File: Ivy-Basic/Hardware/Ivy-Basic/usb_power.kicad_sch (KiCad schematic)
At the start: 1 part, among them J1 USB_C_Receptacle_USB2.0_16P

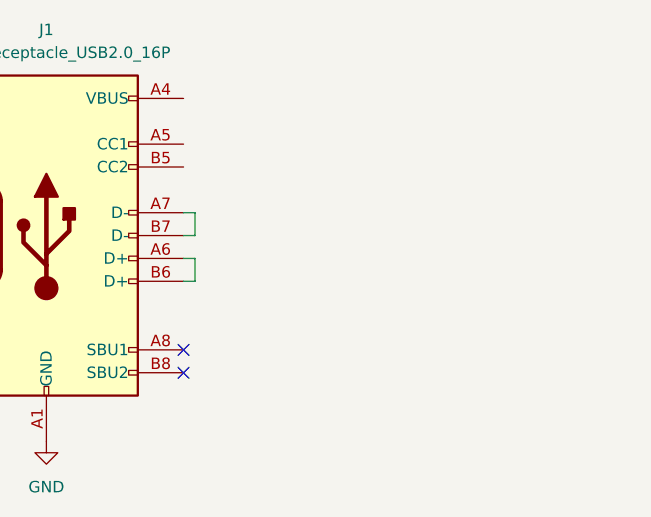
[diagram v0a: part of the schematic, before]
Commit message: Begin USB Power Sheet, ignore file locks, generate symbol library table
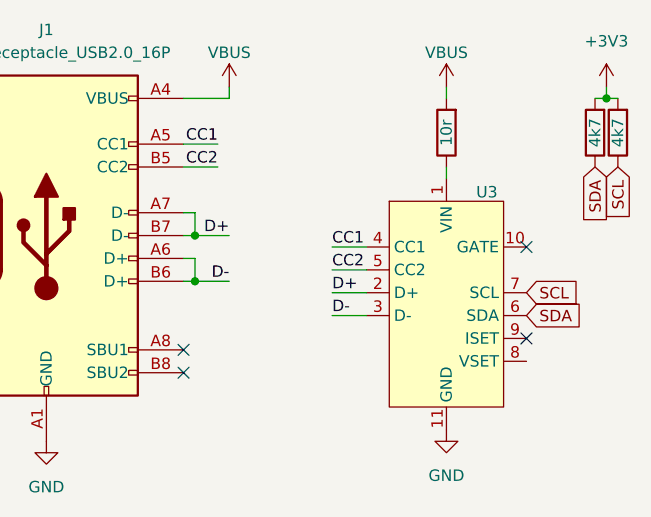
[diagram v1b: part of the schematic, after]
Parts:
- added R1: 10r, symbol Device:R
- added R2, R3: 4k7, symbol Device:R
- added U3: ~, symbol USB_Controller:HUSB238
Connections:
- net GND: now also U3.11 (GND)
- net VBUS: now reaches J1.A4 (VBUS), J1.A9 (VBUS), J1.B4 (VBUS), J1.B9 (VBUS)
- net VBUS: now also R1.2
- net CC1: now reaches J1.A5 (CC1)
- net CC1: now also U3.4 (CC1)
- net D-: now reaches J1.A6 (D+), J1.B6 (D+)
- net D-: now also U3.3 (D-)
- net D+: now reaches J1.A7 (D-), J1.B7 (D-)
- net D+: now also U3.2 (D+)
- net CC2: now reaches J1.B5 (CC2)
- net CC2: now also U3.5 (CC2)
- new net: R1.1, U3.1 (VIN)
- new net +3V3: R2.2, R3.2
- new net SCL: R3.1, U3.7 (SCL)
- new net SDA: R2.1, U3.6 (SDA)
- no-connect marks 2 -> 4

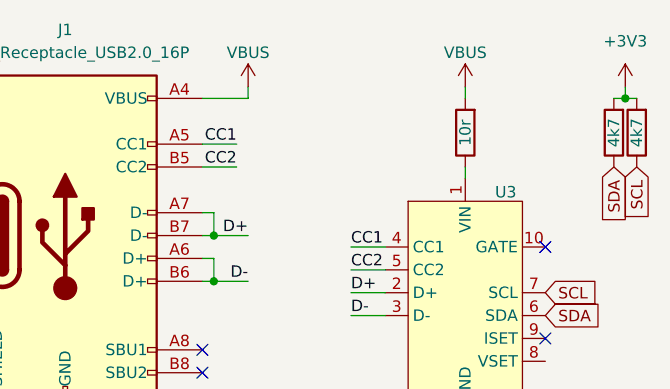
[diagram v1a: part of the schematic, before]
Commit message: USB PD Trigger Complete. Default to 20V.
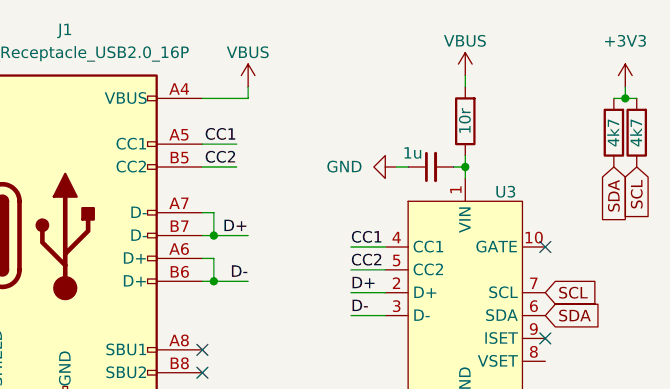
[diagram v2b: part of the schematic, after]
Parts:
- added C1: 1u, Capacitor_SMD:C_0402_1005Metric, symbol Device:C_Small
- J1: footprint (none) -> Connector_USB:USB_C_Receptacle_HRO_TYPE-C-31-M-12
- R1, R2, R3: footprint (none) -> Resistor_SMD:R_0402_1005Metric
- U3: footprint (none) -> Package_DFN_QFN:DFN-10-1EP_3x3mm_P0.5mm_EP1.7x2.5mm
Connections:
- net GND: now also C1.1
- net at R1.1, U3.1 (VIN): now also C1.2
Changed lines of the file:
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@@
+		(color 0 0 0 0)
+	)
+	(junction
+		(at 73.66 29.21)
+		(diameter 0)
 		(color 0 0 0 0)
 	)
@@
 	(wire
 		(pts
-			(xy 73.66 20.32) (xy 73.66 21.59)
+			(xy 72.39 29.21) (xy 73.66 29.21)
+		)
+		(stroke
+			(width 0)
+			(type default)
+		)
+	)
+	(wire
+		(pts
+			(xy 73.66 29.21) (xy 73.66 30.48)
+		)
+		(stroke
+			(width 0)
+			(type default)
+		)
+	)
+	(wire
+		(pts
+			(xy 73.66 19.05) (xy 73.66 20.32)
 		)
 		(stroke
@@
 	(wire
 		(pts
-			(xy 73.66 29.21) (xy 73.66 30.48)
+			(xy 73.66 27.94) (xy 73.66 29.21)
 		)
 		(stroke
@@
 		(pts
 			(xy 64.77 45.72) (xy 60.96 45.72)
+		)
+		(stroke
+			(width 0)
+			(type default)
+		)
+	)
+	(wire
+		(pts
+			(xy 66.04 29.21) (xy 67.31 29.21)
 		)
 		(stroke
@@
 			)
 		)
-		(property "Footprint" ""
+		(property "Footprint" "Package_DFN_QFN:DFN-10-1EP_3x3mm_P0.5mm_EP1.7x2.5mm"
 			(at 73.66 45.72 0)
 			(effects
@@
 			)
 		)
-		(property "Footprint" ""
+		(property "Footprint" "Resistor_SMD:R_0402_1005Metric"
 			(at 94.488 25.4 90)
 			(effects
@@
 			)
 		)
-		(property "Footprint" ""
+		(property "Footprint" "Connector_USB:USB_C_Receptacle_HRO_TYPE-C-31-M-12"
 			(at 33.02 36.83 0)
 			(effects
@@
 			)
 		)
-		(property "Footprint" ""
+		(property "Footprint" "Resistor_SMD:R_0402_1005Metric"
 			(at 91.948 25.4 90)
 			(effects
@@
 	(symbol
 		(lib_id "Device:R")
-		(at 73.66 25.4 180)
+		(at 73.66 24.13 180)
 		(unit 1)
 		(exclude_from_sim no)
@@
 		(dnp no)
 		(property "Reference" "R1"
-			(at 67.31 25.4 90)
+			(at 67.31 24.13 90)
 			(effects
 				(font
@@
 		)
 		(property "Value" "10r"
-			(at 73.66 25.4 90)
-			(effects
-				(font
-					(size 1.27 1.27)
-				)
-			)
-		)
-		(property "Footprint" ""
-			(at 75.438 25.4 90)
+			(at 73.66 24.13 90)
+			(effects
+				(font
+					(size 1.27 1.27)
+				)
+			)
+		)
+		(property "Footprint" "Resistor_SMD:R_0402_1005Metric"
+			(at 75.438 24.13 90)
 			(effects
 				(font
@@
 		)
 		(property "Datasheet" "~"
-			(at 73.66 25.4 0)
+			(at 73.66 24.13 0)
 			(effects
 				(font
@@
 		)
 		(property "Description" "Resistor"
-			(at 73.66 25.4 0)
+			(at 73.66 24.13 0)
 			(effects
 				(font
@@
 				(path "/a769f0bc-ccfa-48fc-9644-27ebf0a18d69/b9c22f62-d201-4347-b849-4fc43ef8bc92"
 					(reference "R1")
+					(unit 1)
+				)
+			)
+		)
+	)
+	(symbol
+		(lib_id "Device:C_Small")
+		(at 69.85 29.21 90)
+		(unit 1)
+		(exclude_from_sim no)
+		(in_bom yes)
+		(on_board yes)
+		(dnp no)
+		(property "Reference" "C1"
+			(at 69.8563 22.86 90)
+			(effects
+				(font
+					(size 1.27 1.27)
+				)
+				(hide yes)
+			)
+		)
+		(property "Value" "1u"
+			(at 67.818 27.686 90)
+			(effects
+				(font
+					(size 1.27 1.27)
+				)
+			)
+		)
+		(property "Footprint" "Capacitor_SMD:C_0402_1005Metric"
+			(at 69.85 29.21 0)
+			(effects
+				(font
+					(size 1.27 1.27)
+				)
+				(hide yes)
+			)
+		)
+		(property "Datasheet" "~"
+			(at 69.85 29.21 0)
+			(effects
+				(font
+					(size 1.27 1.27)
+				)
+				(hide yes)
+			)
+		)
+		(property "Description" "Unpolarized capacitor, small symbol"
+			(at 69.85 29.21 0)
+			(effects
+				(font
+					(size 1.27 1.27)
+				)
+				(hide yes)
+			)
+		)
+		(pin "1"
+		)
+		(pin "2"
+		)
+		(instances
+			(project ""
+				(path "/a769f0bc-ccfa-48fc-9644-27ebf0a18d69/b9c22f62-d201-4347-b849-4fc43ef8bc92"
+					(reference "C1")
 					(unit 1)
 				)
@@
 	(symbol
 		(lib_id "power:VBUS")
-		(at 73.66 20.32 0)
+		(at 73.66 19.05 0)
 		(unit 1)
 		(exclude_from_sim no)
@@
 		(dnp no)
 		(property "Reference" "#PWR05"
-			(at 73.66 24.13 0)
+			(at 73.66 22.86 0)
 			(effects
 				(font
@@
 		)
 		(property "Value" "VBUS"
-			(at 73.66 16.51 0)
+			(at 73.66 15.24 0)
 			(effects
 				(font
@@
 		)
 		(property "Footprint" ""
-			(at 73.66 20.32 0)
+			(at 73.66 19.05 0)
 			(effects
 				(font
@@
 		)
 		(property "Datasheet" ""
-			(at 73.66 20.32 0)
+			(at 73.66 19.05 0)
 			(effects
 				(font
@@
 		)
 		(property "Description" "Power symbol creates a global label with name \"VBUS\""
-			(at 73.66 20.32 0)
+			(at 73.66 19.05 0)
 			(effects
 				(font
@@
 					(unit 1)
 				)
+			)
+		)
+	)
+	(symbol
+		(lib_id "power:GND")
+		(at 66.04 29.21 270)
+		(unit 1)
+		(exclude_from_sim no)
+		(in_bom yes)
+		(on_board yes)
+		(dnp no)
+		(fields_autoplaced yes)
+		(property "Reference" "#PWR07"
+			(at 59.69 29.21 0)
+			(effects
+				(font
+					(size 1.27 1.27)
+				)
+				(hide yes)
+			)
+		)
+		(property "Value" "GND"
+			(at 62.23 29.2099 90)
+			(effects
+				(font
+					(size 1.27 1.27)
+				)
+				(justify right)
+			)
+		)
+		(property "Footprint" ""
+			(at 66.04 29.21 0)
+			(effects
+				(font
+					(size 1.27 1.27)
+				)
+				(hide yes)
+			)
+		)
+		(property "Datasheet" ""
+			(at 66.04 29.21 0)
+			(effects
+				(font
+					(size 1.27 1.27)
+				)
+				(hide yes)
+			)
+		)
+		(property "Description" "Power symbol creates a global label with name \"GND\" , ground"
+			(at 66.04 29.21 0)
+			(effects
+				(font
+					(size 1.27 1.27)
+				)
+				(hide yes)
+			)
+		)
+		(pin "1"
+		)
+		(instances
+			(project ""
+				(path "/a769f0bc-ccfa-48fc-9644-27ebf0a18d69/b9c22f62-d201-4347-b849-4fc43ef8bc92"
+					(reference "#PWR07")
+					(unit 1)
+				)

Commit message: ti switcher
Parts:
- added C10, C11: 100n, Capacitor_SMD:C_0402_1005Metric, symbol Device:C_Small
- added IC1: LMR54406DBVR, SOT95P280X145-6N, symbol LMR54406DBVR:LMR54406DBVR
- added L1: 10u, symbol Device:L
- added R5: 69k8, symbol Device:R
- added R6: 22k1, symbol Device:R
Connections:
- net +3V3: now also L1.2, R5.2
- net GND: now also C11.1, IC1.2 (GND), R6.1
- net VBUS: now also C11.2, IC1.4 (EN), IC1.5 (VIN)
- new net: C10.1, IC1.1 (CB)
- new net: C10.2, IC1.6 (SW), L1.1
- new net FB: IC1.3 (FB), R5.1, R6.2

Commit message: Replace buck converter with something that might work better
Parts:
- added C12: 10u, Capacitor_SMD:C_0603_1608Metric, symbol Device:C_Small
- added D1: D, Diode_SMD:D_SOD-123, symbol Device:D
- added R10: 100k, Resistor_SMD:R_0402_1005Metric, symbol Device:R
- C11: value 100n -> 4u7; footprint Capacitor_SMD:C_0402_1005Metric -> Capacitor_SMD:C_0603_1608Metric
- IC1: value LMR54406DBVR -> SSP9451; footprint SOT95P280X145-6N -> Package_TO_SOT_SMD:SOT-23-6; Height 1.45 -> (none); LCSC (none) -> C411009; Manufacturer_Name Texas Instruments -> (none); Manufacturer_Part_Number LMR54406DBVR -> (none); Mouser Part Number 595-LMR54406DBVR -> (none); Mouser Price/Stock https://www.mouser.co.uk/ProductDetail/Texas-Instruments/LM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 -> (none)
- L1: value 10u -> 3u3; footprint (none) -> Inductor_SMD:L_Abracon_ASPI-0425
- R5: value 69k8 -> 124k; footprint (none) -> Resistor_SMD:R_0402_1005Metric
- R6: value 22k1 -> 40k2; footprint (none) -> Resistor_SMD:R_0402_1005Metric
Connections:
- net +3V3: now also C12.2
- net GND: now also C12.1, D1.2 (A)
- net VBUS: now also R10.2; no longer IC1.4 (EN)
- net at C10.2, IC1.6 (SW), L1.1: now also D1.1 (K)
- new net: IC1.4 (EN), R10.1
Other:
- note added: "3v3 regulator. 6-24v in."
- note added: "PD Trigger. Nominally 20v."
- moved on the sheet: IC1

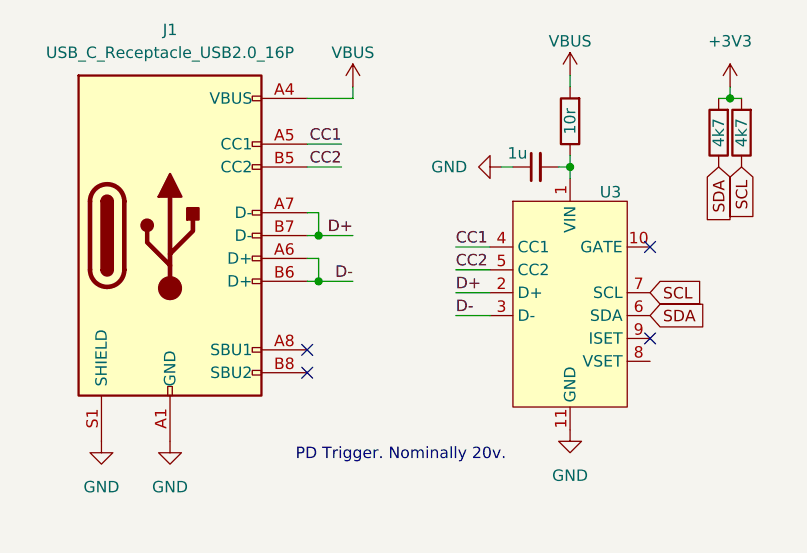
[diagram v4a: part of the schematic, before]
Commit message: Add 3D models, set board outline, place USB input, ESP32, Buck Converter
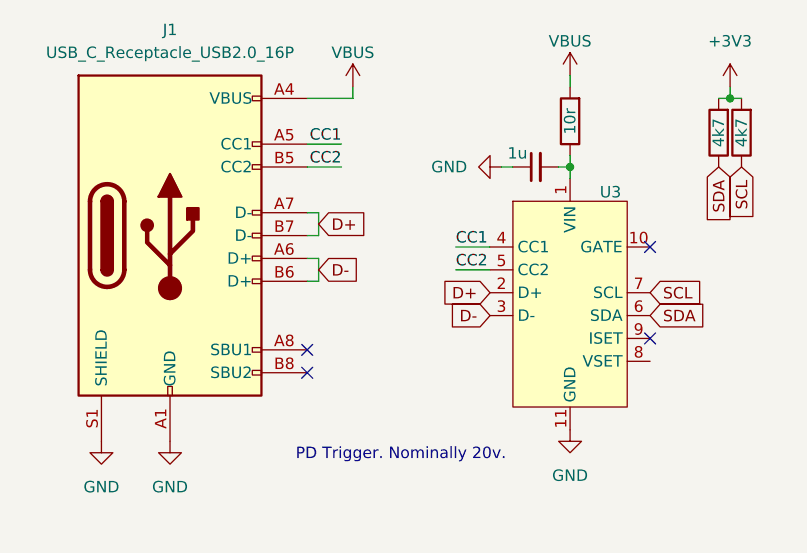
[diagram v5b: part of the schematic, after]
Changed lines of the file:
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@@
-	)
-	(junction
-		(at 45.72 41.91)
-		(diameter 0)
-		(color 0 0 0 0)
-	)
-	(junction
-		(at 45.72 36.83)
-		(diameter 0)
-		(color 0 0 0 0)
 	)
 	(junction
@@
 	(wire
 		(pts
-			(xy 64.77 43.18) (xy 60.96 43.18)
-		)
-		(stroke
-			(width 0)
-			(type default)
-		)
-	)
-	(wire
-		(pts
 			(xy 73.66 27.94) (xy 73.66 29.21)
 		)
@@
 	(wire
 		(pts
-			(xy 45.72 41.91) (xy 49.53 41.91)
-		)
-		(stroke
-			(width 0)
-			(type default)
-		)
-	)
-	(wire
-		(pts
 			(xy 44.45 41.91) (xy 45.72 41.91)
 		)
@@
 	(wire
 		(pts
-			(xy 64.77 45.72) (xy 60.96 45.72)
-		)
-		(stroke
-			(width 0)
-			(type default)
-		)
-	)
-	(wire
-		(pts
 			(xy 66.04 29.21) (xy 67.31 29.21)
 		)
@@
 		(pts
 			(xy 44.45 36.83) (xy 45.72 36.83)
-		)
-		(stroke
-			(width 0)
-			(type default)
-		)
-	)
-	(wire
-		(pts
-			(xy 45.72 36.83) (xy 49.53 36.83)
 		)
 		(stroke
@@
 		)
 	)
-	(label "D+"
-		(at 49.53 36.83 180)
-		(fields_autoplaced yes)
-		(effects
-			(font
-				(size 1.27 1.27)
-			)
-			(justify right bottom)
-		)
-	)
 	(label "CC2"
 		(at 60.96 40.64 0)
@@
 		)
 	)
-	(label "D-"
-		(at 60.96 45.72 0)
-		(fields_autoplaced yes)
-		(effects
-			(font
-				(size 1.27 1.27)
-			)
-			(justify left bottom)
-		)
-	)
-	(label "D-"
-		(at 49.53 41.91 180)
-		(fields_autoplaced yes)
-		(effects
-			(font
-				(size 1.27 1.27)
-			)
-			(justify right bottom)
-		)
-	)
 	(label "CC1"
 		(at 60.96 38.1 0)
@@
 		)
 	)
-	(label "D+"
-		(at 60.96 43.18 0)
-		(fields_autoplaced yes)
-		(effects
-			(font
-				(size 1.27 1.27)
-			)
-			(justify left bottom)
-		)
-	)
 	(global_label "SCL"
 		(shape input)
@@
 		)
 	)
+	(global_label "D+"
+		(shape input)
+		(at 64.77 43.18 180)
+		(fields_autoplaced yes)
+		(effects
+			(font
+				(size 1.27 1.27)
+			)
+			(justify right)
+		)
+		(property "Intersheetrefs" "${INTERSHEET_REFS}"
+			(at 58.9424 43.18 0)
+			(effects
+				(font
+					(size 1.27 1.27)
+				)
+				(justify right)
+				(hide yes)
+			)
+		)
+	)
 	(global_label "SDA"
 		(shape input)
@@
 		)
 	)
+	(global_label "D+"
+		(shape input)
+		(at 45.72 35.56 0)
+		(fields_autoplaced yes)
+		(effects
+			(font
+				(size 1.27 1.27)
+			)
+			(justify left)
+		)
+		(property "Intersheetrefs" "${INTERSHEET_REFS}"
+			(at 51.5476 35.56 0)
+			(effects
+				(font
+					(size 1.27 1.27)
+				)
+				(justify left)
+				(hide yes)
+			)
+		)
+	)
 	(global_label "FB"
 		(shape input)
@@
 		)
 	)
+	(global_label "D-"
+		(shape input)
+		(at 45.72 40.64 0)
+		(fields_autoplaced yes)
+		(effects
+			(font
+				(size 1.27 1.27)
+			)
+			(justify left)
+		)
+		(property "Intersheetrefs" "${INTERSHEET_REFS}"
+			(at 51.5476 40.64 0)
+			(effects
+				(font
+					(size 1.27 1.27)
+				)
+				(justify left)
+				(hide yes)
+			)
+		)
+	)
 	(global_label "FB"
 		(shape input)
@@
 				(hide yes)
 			)
+		)
+	)
+	(global_label "D-"
+		(shape input)
+		(at 64.77 45.72 180)
+		(fields_autoplaced yes)
+		(effects
+			(font
+				(size 1.27 1.27)
+			)
+			(justify right)
+		)
+		(property "Intersheetrefs" "${INTERSHEET_REFS}"
+			(at 58.9424 45.72 0)
+			(effects
+				(font
+					(size 1.27 1.27)
+				)
+				(justify right)
+				(hide yes)
+			)
